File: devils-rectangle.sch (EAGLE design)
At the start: 22 parts, among them J3 CORTEX_DEBUG_PTH, J6 USB-MICROB, U1 ATSAMD21G-M, U2 MIC5501-3.0YM5-TR, U3 TPD2S017

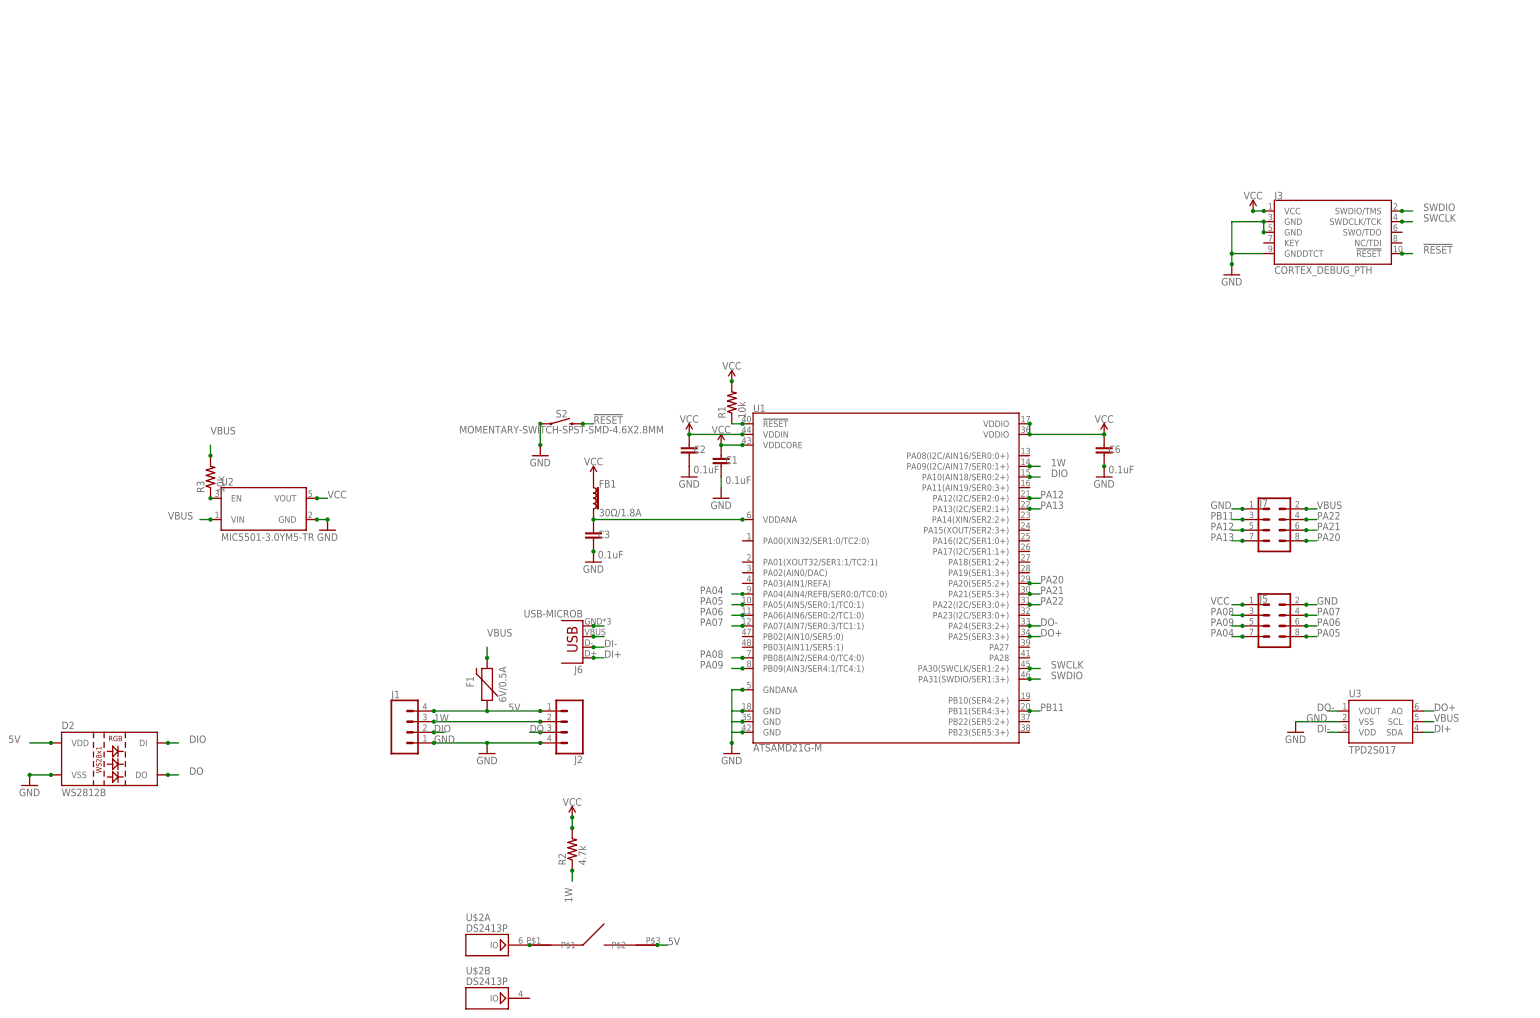
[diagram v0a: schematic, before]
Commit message: updated gitignore and renamed project `
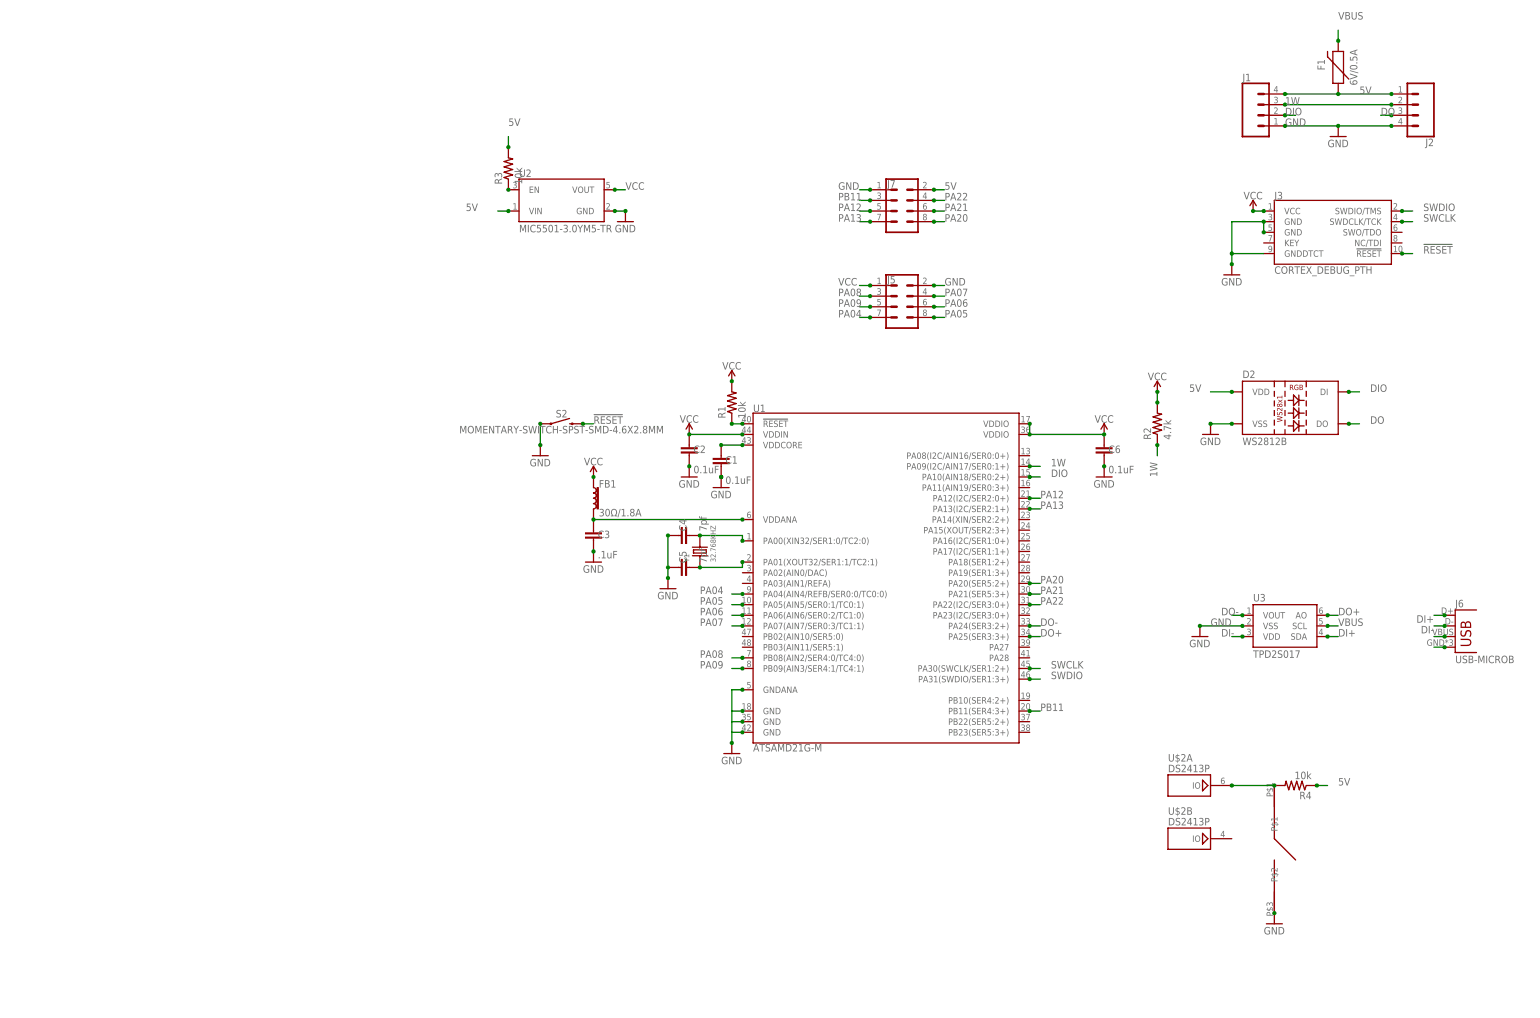
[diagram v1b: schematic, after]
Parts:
- added C4, C5: 7pf, SparkFun-Capacitors:0.1UF-0402-16V-10%
- added R4: 10k, rcl:R-US_R0402
- added Y1: 32.768KHZ, Seeed-Crystal Oscillator:SMD-CRYSTAL-ABS07-32.768KHZ-7PF-20PPM-70K(2P-3.2X1.5MM)
- C3: value 0.1uF -> .1uF
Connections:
- new net N$12: C5.2, U1.PA01(XOUT32/SER1:1/TC2:1), Y1.1
- new net N$13: C4.2, U1.PA00(XIN32/SER1:0/TC2:0), Y1.2
- new net N$14: C1.1, U1.VDDCORE
- net 5V: now also J7.2, R3.2, R4.1, U2.VIN; no longer U$1.P$2
- net GND: now also C4.1, C5.1, U$1.P$2
- net N$10: now also R4.2
- net VBUS: no longer J7.2, R3.2, U2.VIN
- net VCC: no longer C1.1, U1.VDDCORE
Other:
- moved on the sheet: D2, F1, J1, J2, J5, J6, J7, R2, R3, U$2A, U$2B, U2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

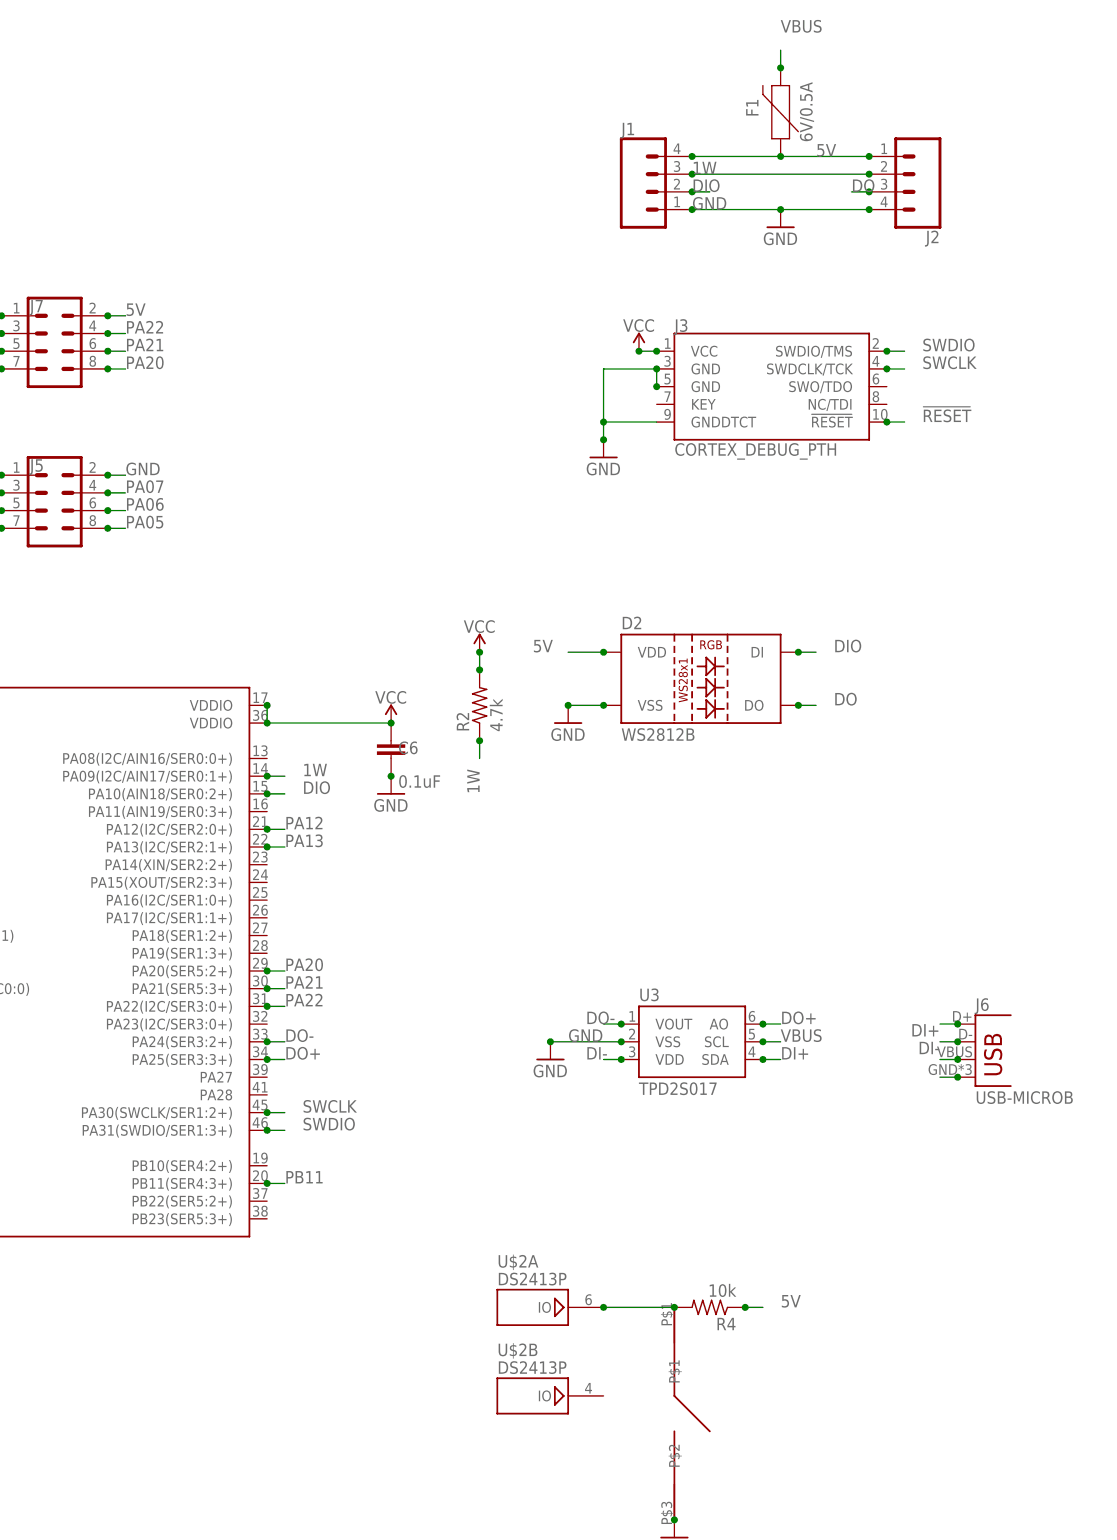
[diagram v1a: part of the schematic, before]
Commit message: updated bus switch
updated bus switch to i2c to resolve arduino zero issue with onewire
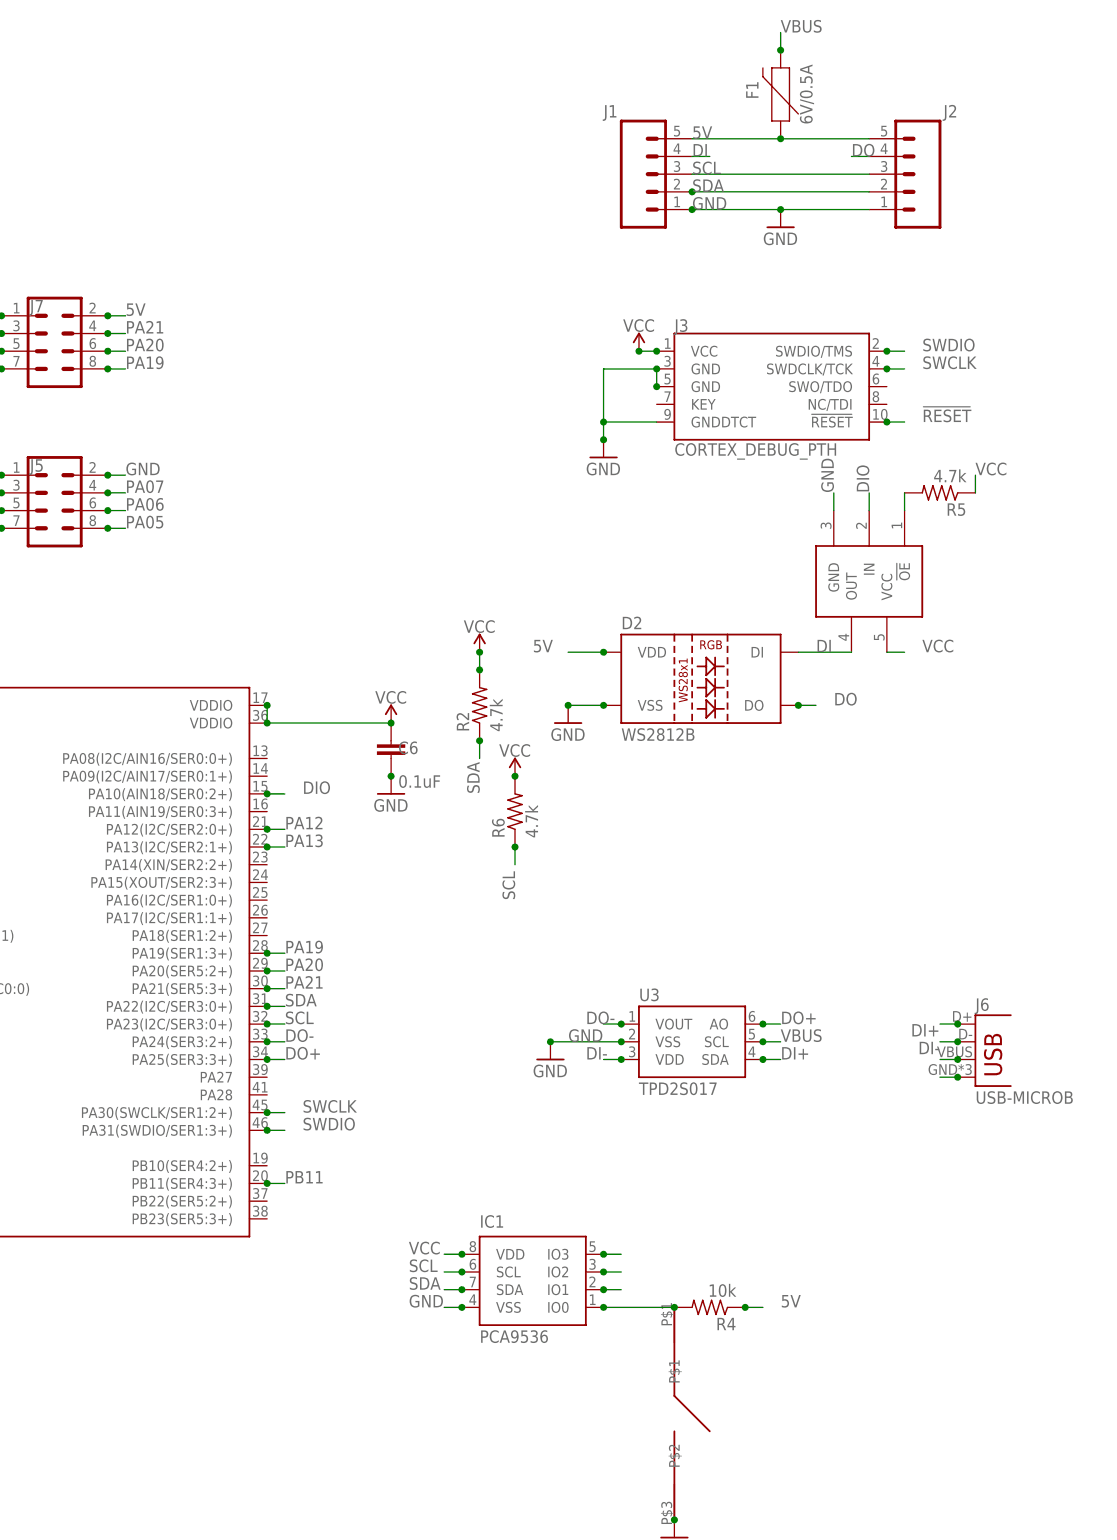
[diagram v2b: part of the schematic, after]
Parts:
- removed U$2: DS2413P, 1wire:DS2413P
- added IC1: PCA9536, PCA9536:PCA9536
- added R5, R6: 4.7k, rcl:R-US_R0402
- added U$3: M74VHC1GT125, MC74VHC1GT125:M74VHC1GT125
- J1, J2: device SparkFun-Connectors:CONN_04SMD2 -> SparkFun-Connectors:CONN_05SMD
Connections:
- removed net 1W: J1.3, J2.2, R2.1, U1.PA09(I2C/AIN17/SER0:1+)
- removed net PA22: J7.4, U1.PA22(I2C/SER3:0+)
- new net DI: D2.DI, J1.4, U$3.OUT
- new net N$19: R5.2, U$3.!OE
- new net N$20: IC1.IO1
- new net N$21: IC1.IO2
- new net N$22: IC1.IO3
- new net PA19: J7.8, U1.PA19(SER1:3+)
- new net SCL: IC1.SCL, J1.3, J2.3, R6.1, U1.PA23(I2C/SER3:0+)
- new net SDA: IC1.SDA, J1.2, J2.2, R2.1, U1.PA22(I2C/SER3:0+)
- net 5V: now also J1.5, J2.5; no longer J1.4, J2.1
- net DIO: now also U$3.IN; no longer D2.DI, J1.2
- net DO: now also J2.4; no longer J2.3
- net GND: now also IC1.VSS, J2.1, U$3.GND; no longer J2.4
- net N$10: now also IC1.IO0; no longer U$2A.IO
- net PA20: now also J7.6; no longer J7.8
- net PA21: now also J7.4; no longer J7.6
- net VCC: now also IC1.VDD, R5.1, R6.2, U$3.VCC
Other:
- moved on the sheet: F1

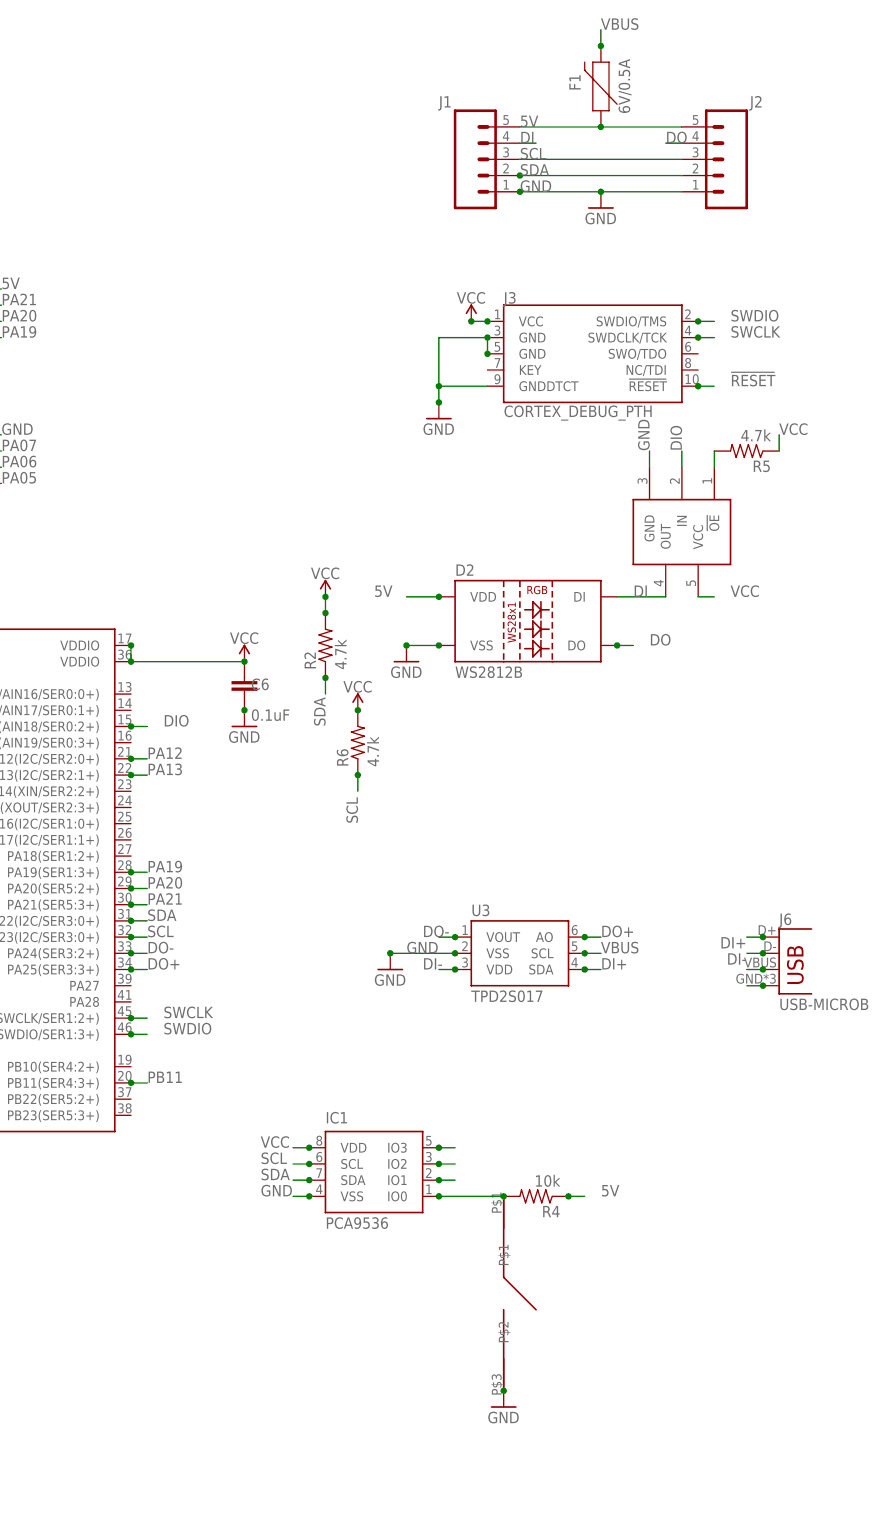
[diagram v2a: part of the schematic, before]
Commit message: replaced i2c port expander
replaced i2c port expander with an attiny85. added 3v pin to daughter board header.
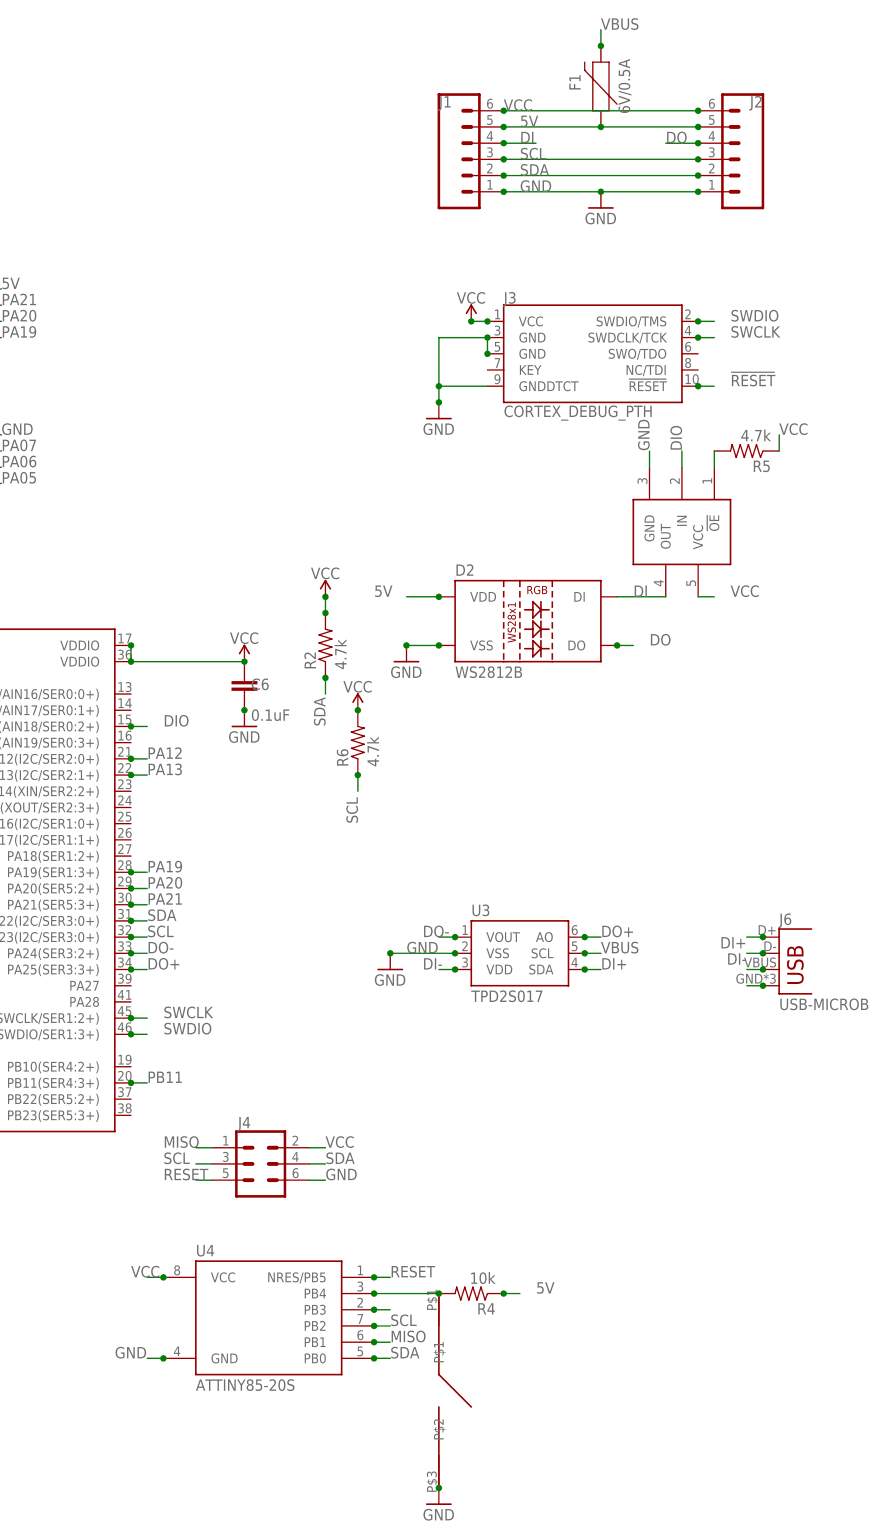
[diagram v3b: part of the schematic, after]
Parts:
- removed IC1: PCA9536, PCA9536:PCA9536
- added J4: (no value), SparkFun-Connectors:CONN_03X22X3_SILK_MALE_PTH
- added U4: ATTINY85-20S, _hhn_attiny25_45_85:ATTINY85-20S
- J1, J2: device SparkFun-Connectors:CONN_05SMD -> SparkFun-Connectors:CONN_06SMD-1MM
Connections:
- removed net N$20: IC1.IO1
- removed net N$22: IC1.IO3
- new net MISO: J4.1, U4.PB1
- new net RESET: J4.5, U4.NRES/PB5
- net GND: now also J4.6, U4.GND; no longer IC1.VSS
- net N$10: now also U4.PB4; no longer IC1.IO0
- net N$21: now also U4.PB3; no longer IC1.IO2
- net SCL: now also J4.3, U4.PB2; no longer IC1.SCL
- net SDA: now also J4.4, U4.PB0; no longer IC1.SDA
- net VCC: now also J1.6, J2.6, J4.2, U4.VCC; no longer IC1.VDD
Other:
- moved on the sheet: R4
